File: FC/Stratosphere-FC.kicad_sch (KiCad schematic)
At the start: 46 parts, among them J1 Conn_01x04, P2 USB_C_Plug_USB2.0, U1 ICM-42605, U2 W25Q16JVSS, U3 BMP388, U4 XC6206P332MR, U8 STM32F405RGTx, X2 Shenzhen SCTF Elec SX2B12.000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

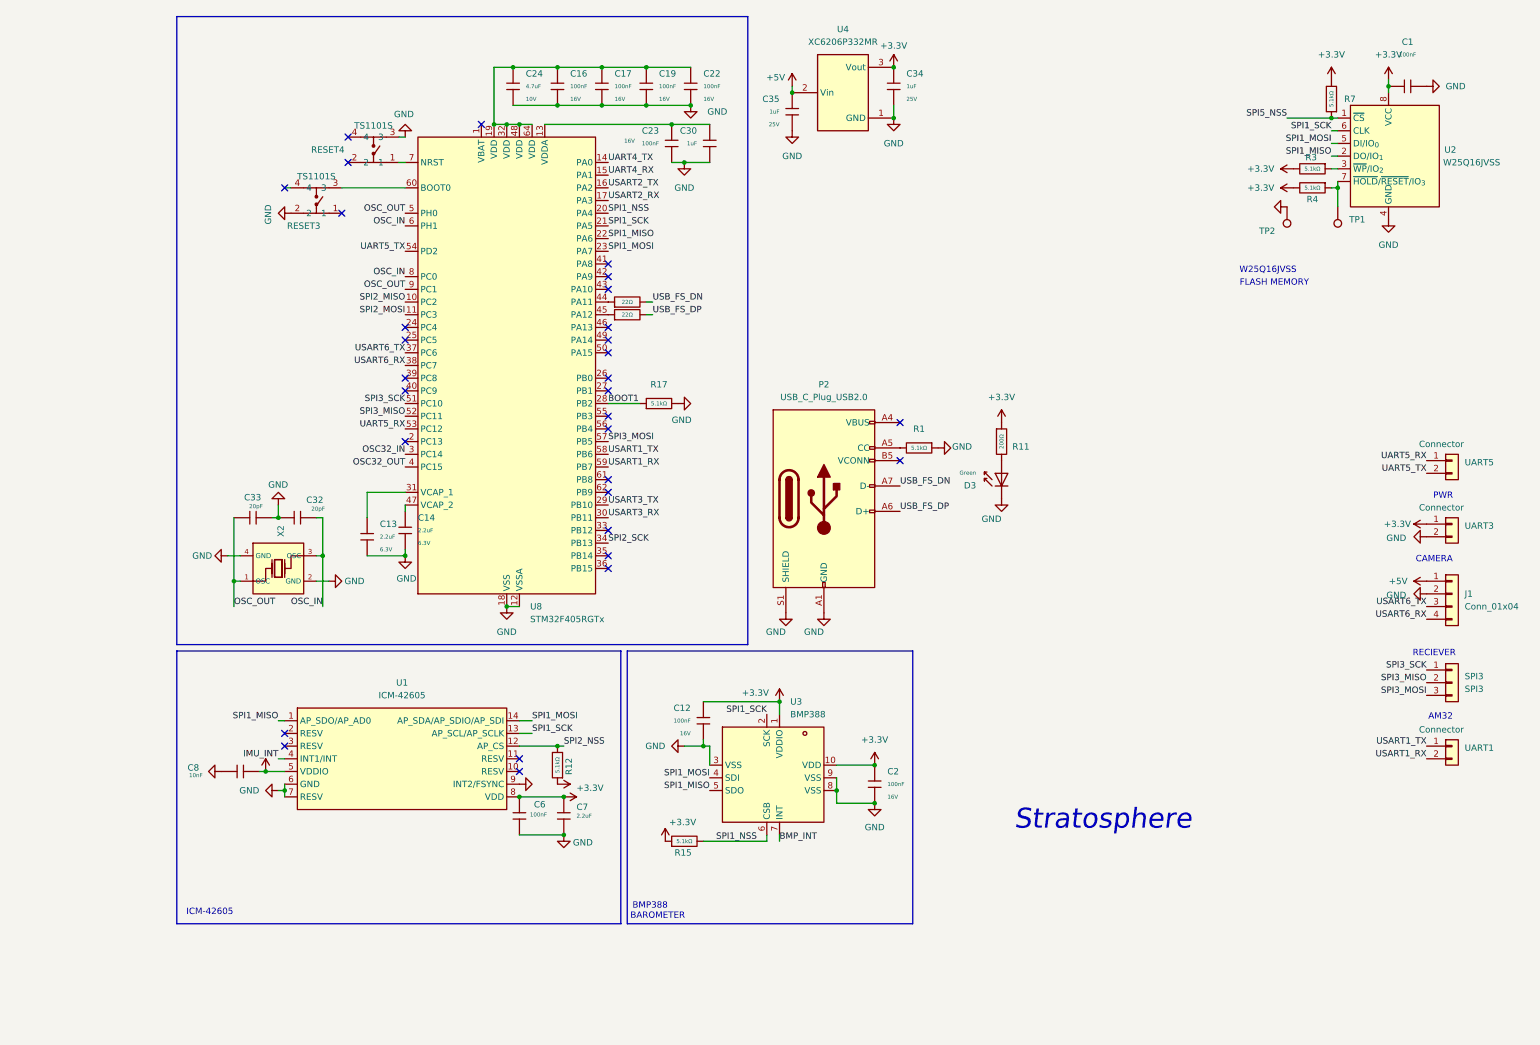
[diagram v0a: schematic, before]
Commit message: Feat: Addition of Power Module Schematic PCB
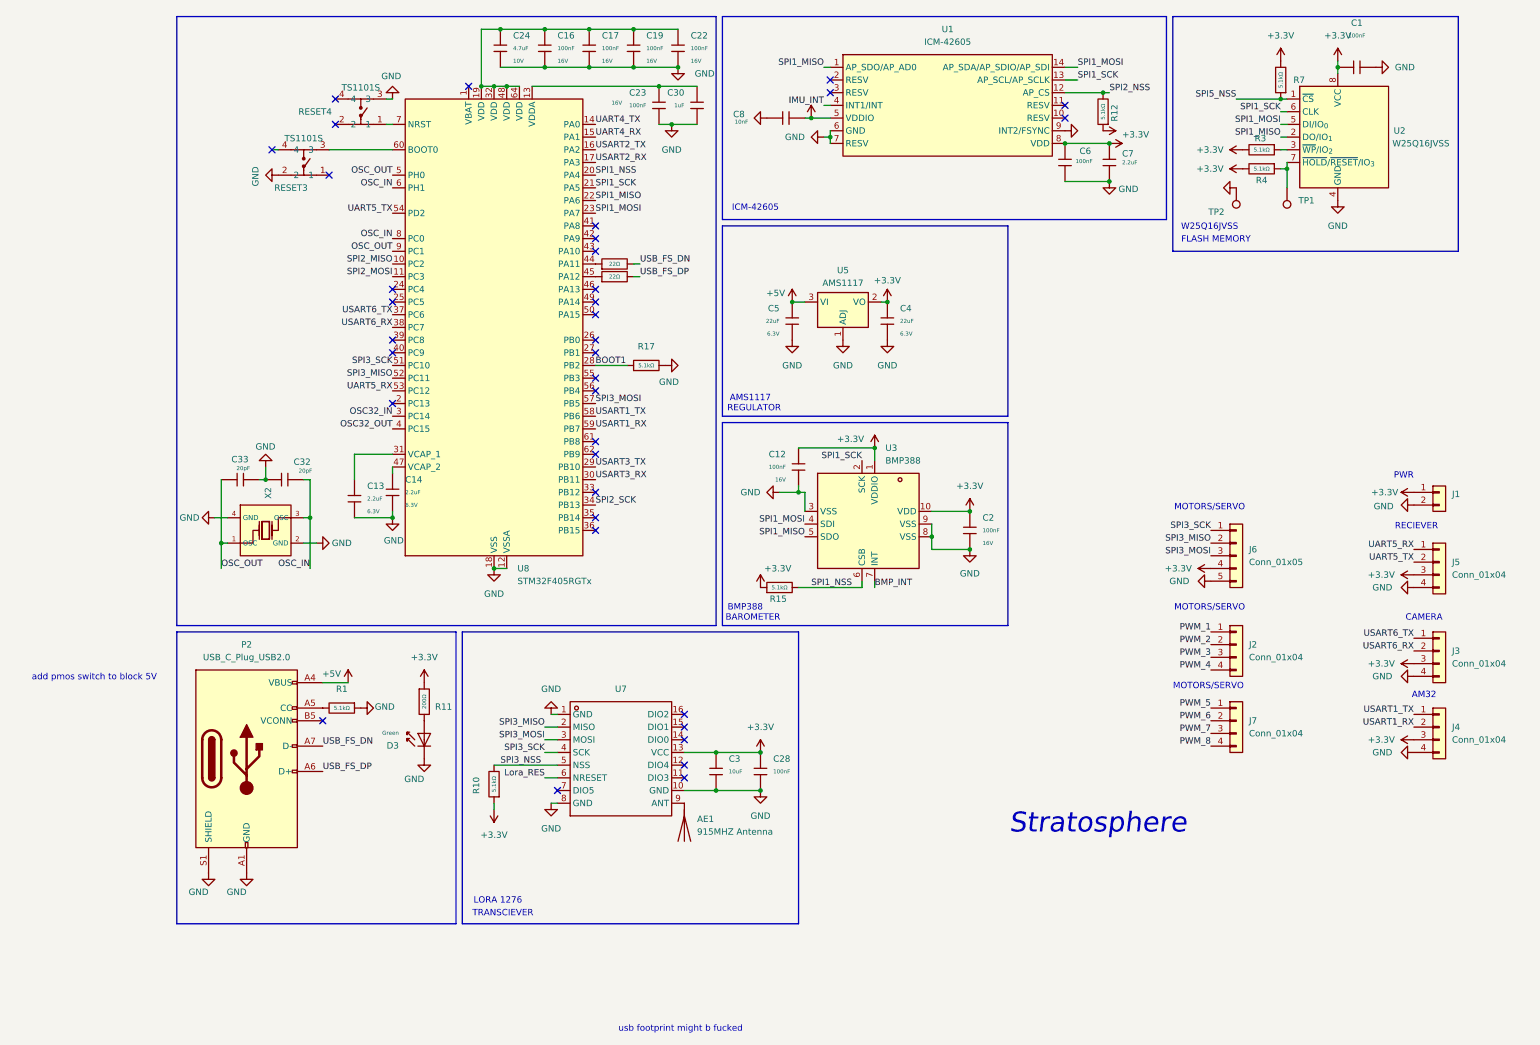
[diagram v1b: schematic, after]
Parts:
- removed C34, C35: 1uF, PCM_JLCPCB:C_0402, symbol PCM_JLCPCB-Capacitors:0402,1uF
- removed J1: Conn_01x04, Connector_JST:JST_GH_SM04B-GHS-TB_1x04-1MP_P1.25mm_Horizontal, symbol Connector_Generic:Conn_01x04
- removed SPI3: SPI3, Connector_JST:JST_GH_SM03B-GHS-TB_1x03-1MP_P1.25mm_Horizontal, symbol Connector_Generic:Conn_01x03
- removed U4: XC6206P332MR, easyeda2kicad:SOT-23-3_L2.9-W1.6-P1.90-LS2.8-BR, symbol easyeda2kicad:XC6206P332MR
- removed UART1, UART5: Connector, JST_GH_SM02B-GHS-TB_1x02-1MP_P1.25mm_Horizontal, symbol Connector_Generic_MountingPin:Conn_01x02_MountingPin
- added AE1: 915MHZ Antenna, Connector_Coaxial:U.FL_Molex_MCRF_73412-0110_Vertical, symbol Device:Antenna
- added C28: 100nF, PCM_JLCPCB:C_0402, symbol PCM_JLCPCB-Capacitors:0402,100nF
- added C3: 10uF, PCM_JLCPCB:C_0402, symbol PCM_JLCPCB-Capacitors:0402,10uF
- added C4, C5: 22uF, PCM_JLCPCB:C_0603, symbol PCM_JLCPCB-Capacitors:0603,22uF
- added J2, J3, J4, J5, J7: Conn_01x04, Connector_JST:JST_GH_SM04B-GHS-TB_1x04-1MP_P1.25mm_Horizontal, symbol Connector_Generic:Conn_01x04
- added J6: Conn_01x05, Connector_JST:JST_GH_BM05B-GHS-TBT_1x05-1MP_P1.25mm_Vertical, symbol Connector_Generic:Conn_01x05
- added R10: 5.1kΩ, PCM_JLCPCB:R_0402, symbol PCM_JLCPCB-Resistors:0402,5.1kΩ
- added U5: AMS1117, Package_TO_SOT_SMD:SOT-223-3_TabPin2, symbol Regulator_Linear:AMS1117
- added U7: 915MHz, lib:COMM-SMD_LORA1276-C1-915MHZ, symbol lora1276:LORA1276-C1-915MHZ
- renumbered UART3 to J1
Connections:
- net +3.3V: now also C28.1, C3.1, C4.1, J3.3 (Pin_3), J4.3 (Pin_3), J5.3 (Pin_3), J6.4 (Pin_4), R10.1, U5.2 (VO), U7.13 (VCC)
- net +5V: now also P2.A4 (VBUS), P2.A9 (VBUS), P2.B4 (VBUS), P2.B9 (VBUS), C5.1, U5.3 (VI)
- net GND: now also C28.2, C3.2, C4.2, C5.2, J3.4 (Pin_4), J4.4 (Pin_4), J5.4 (Pin_4), J6.5 (Pin_5), U5.1 (ADJ), U7.1 (GND), U7.10 (GND), U7.8 (GND)
- net SPI3_MISO: now also J6.2 (Pin_2), U7.2 (MISO)
- net SPI3_MOSI: now also J6.3 (Pin_3), U7.3 (MOSI)
- net SPI3_SCK: now also J6.1 (Pin_1), U7.4 (SCK)
- net UART5_RX: now also J5.1 (Pin_1)
- net UART5_TX: now also J5.2 (Pin_2)
- net USART1_RX: now also J4.2 (Pin_2)
- net USART1_TX: now also J4.1 (Pin_1)
- net USART6_RX: now also J3.2 (Pin_2)
- net USART6_TX: now also J3.1 (Pin_1)
- new net: AE1.1 (A), U7.9 (ANT)
- new net Lora_RES: U7.6 (NRESET)
- new net PWM_1: J2.1 (Pin_1)
- new net PWM_2: J2.2 (Pin_2)
- new net PWM_3: J2.3 (Pin_3)
- new net PWM_4: J2.4 (Pin_4)
- new net PWM_5: J7.1 (Pin_1)
- new net PWM_6: J7.2 (Pin_2)
- new net PWM_7: J7.3 (Pin_3)
- new net PWM_8: J7.4 (Pin_4)
- new net SPI3_NSS: R10.2, U7.5 (NSS)
- no-connect marks 31 -> 36
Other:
- note added: "AMS1117"
- note added: "LORA 1276"
- note added: "MOTORS/SERVO"
- note added: "REGULATOR"
- note added: "TRANSCIEVER"
- note added: "add pmos switch to block 5V"
- note added: "usb footprint might b fucked"
- moved on the sheet: C1, C12, C13, C14, C16, C17, C19, C2, C22, C23, C24, C30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

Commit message: fix: updated connector, horzontal to vertical
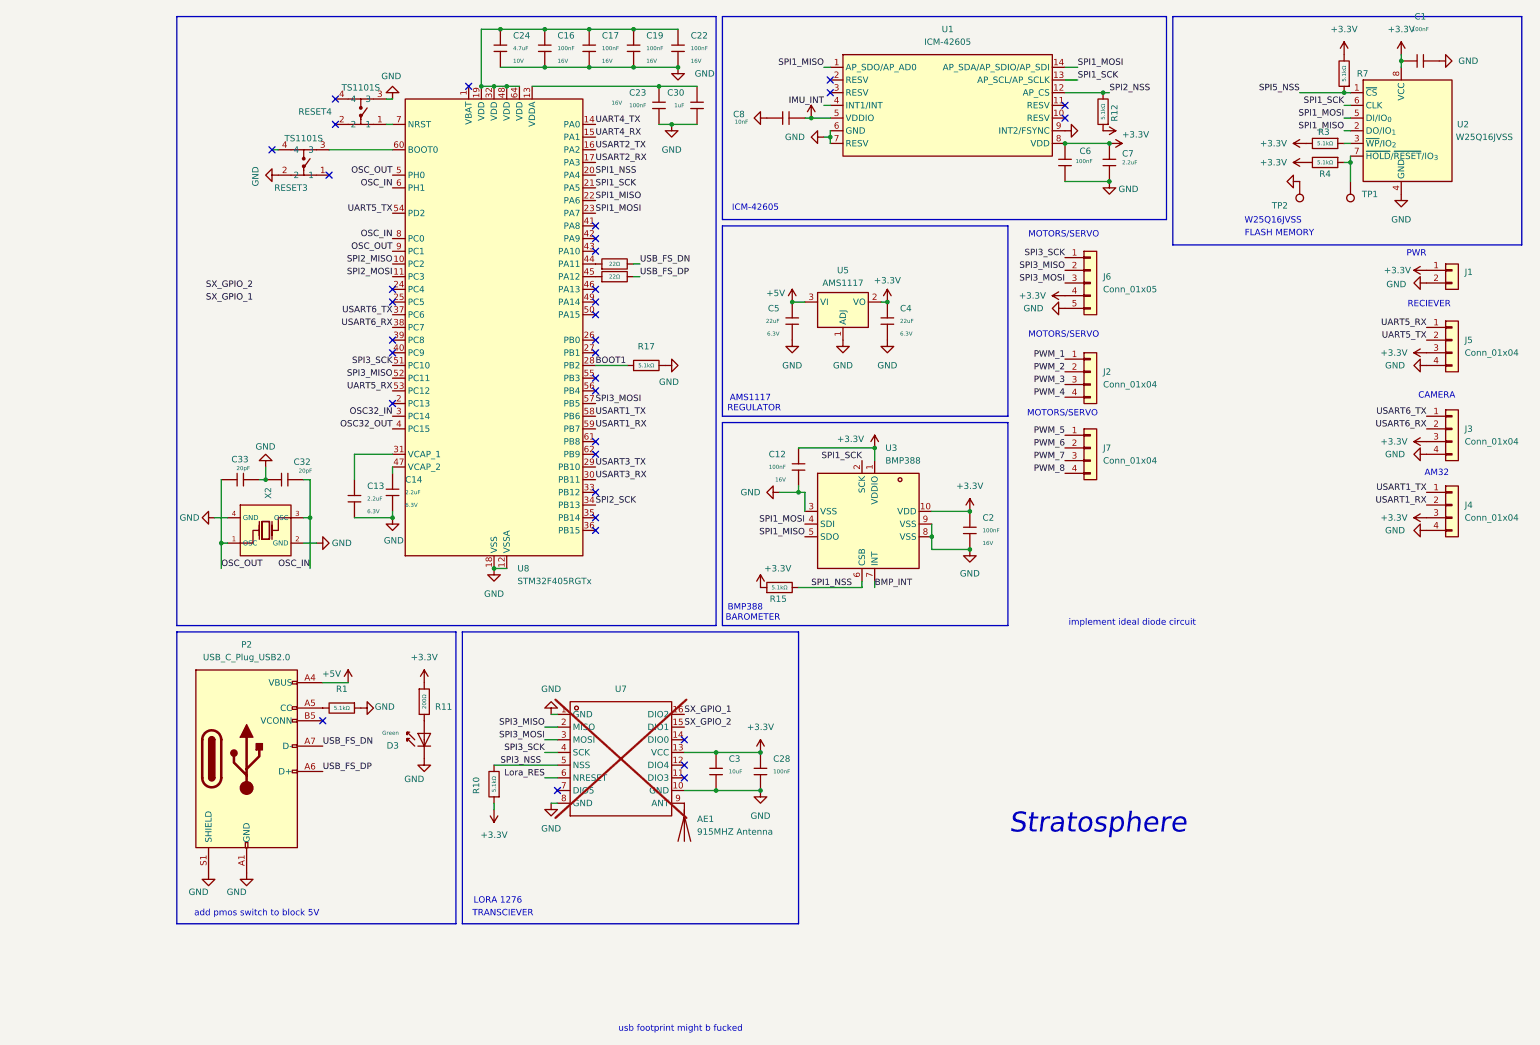
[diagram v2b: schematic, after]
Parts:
- AE1: footprint Connector_Coaxial:U.FL_Molex_MCRF_73412-0110_Vertical -> Connector_Coaxial:SMA_Amphenol_901-144_Vertical
- J1: footprint JST_GH_SM02B-GHS-TB_1x02-1MP_P1.25mm_Horizontal -> Connector_JST:JST_GH_BM02B-GHS-TBT_1x02-1MP_P1.25mm_Vertical
- J2, J3, J4, J5, J7: footprint Connector_JST:JST_GH_SM04B-GHS-TB_1x04-1MP_P1.25mm_Horizontal -> Connector_JST:JST_GH_BM04B-GHS-TBT_1x04-1MP_P1.25mm_Vertical
- U7: now not fitted
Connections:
- net SX_GPIO_2: now reaches U7.15 (DIO1)
- net SX_GPIO_1: now reaches U7.16 (DIO2)
- no-connect marks 36 -> 34
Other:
- note added: "implement ideal diode circuit"
- moved on the sheet: C1, J1, J2, J3, J4, J5, J6, J7, R3, R4, R7, TP1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
